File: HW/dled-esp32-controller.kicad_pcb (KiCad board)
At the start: 2 copper layers, 50 x 48 mm, 40 parts, among them J1 PinsI2C, J2 PinsDbg, J3 BootBtn, J4 swRes, J5 LEDcmd, J6 PinsExt, J7 PinsExt2, J8 LEDpwr, J9 Power5V, Q1 STD46P4LLF6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

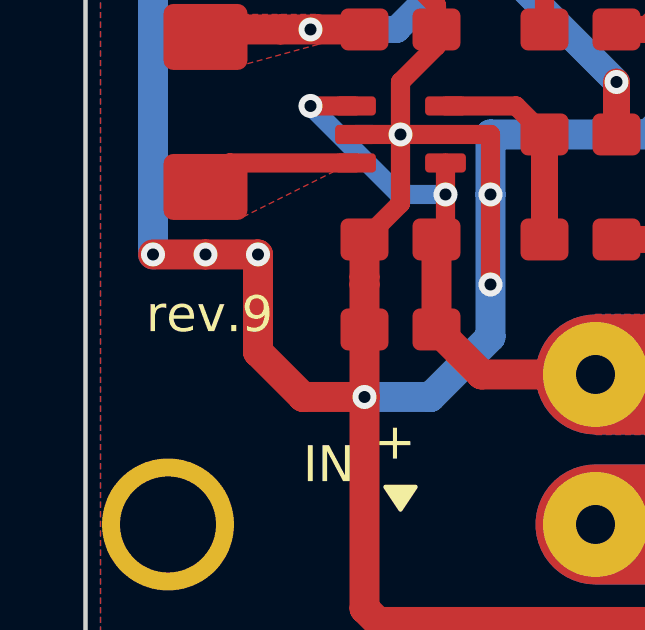
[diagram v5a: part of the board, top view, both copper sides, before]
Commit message: Changes the 3D representation of some connectors
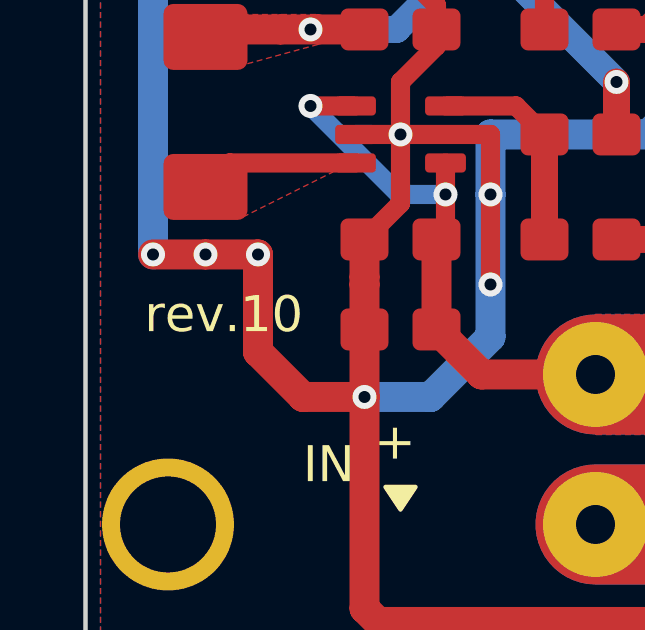
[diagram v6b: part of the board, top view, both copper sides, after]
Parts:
- J2: footprint CalinConnectors:Pin_Header_Straight_1x03 -> CalinConnectors:Pin_Header_Straight_1x03_Cyan
- J5: footprint CalinConnectors:Pin_Header_Straight_1x03 -> CalinConnectors:Pin_Header_Straight_1x03_Yellow
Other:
- board text added: "rev.10"
- board text removed: "rev.9"

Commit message: Rebuilds the PCB for revision 11
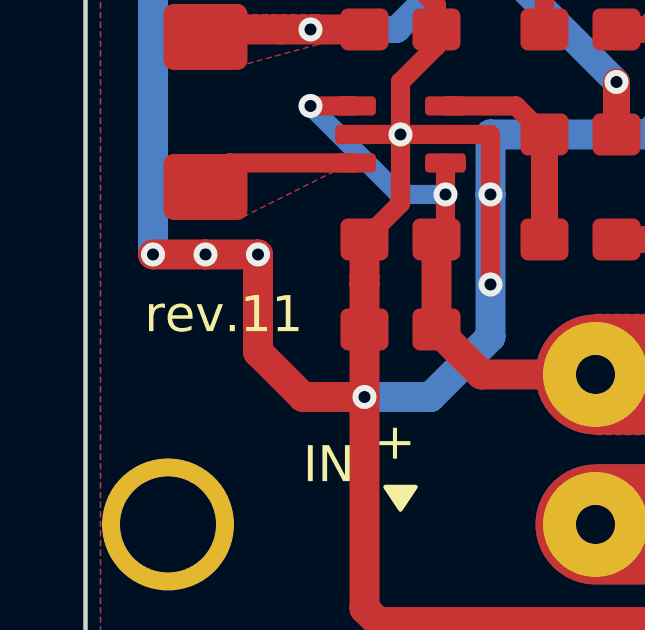
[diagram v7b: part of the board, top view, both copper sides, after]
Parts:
- L1: value 1uH -> 2.2uH
- R2: value 1k -> 330
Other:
- board text added: "rev.11"
- board text removed: "rev.10"
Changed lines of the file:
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@@
       (effects (font (size 1 1) (thickness 0.15)))
     )
-    (fp_text value 1uH (at 0 -3.4 90) (layer F.Fab)
+    (fp_text value 2.2uH (at 0 -3.4 90) (layer F.Fab)
       (effects (font (size 1 1) (thickness 0.15)))
     )
@@
       (effects (font (size 1 1) (thickness 0.15)))
     )
-    (fp_text value 1k (at 0 -2 180) (layer F.Fab)
+    (fp_text value 330 (at 0 -2 180) (layer F.Fab)
       (effects (font (size 1 1) (thickness 0.15)))
     )
@@
     )
   )
-  (gr_text rev.10 (at 32.25 88.5) (layer F.SilkS)
+  (gr_text rev.11 (at 32.25 88.5) (layer F.SilkS)
     (effects (font (size 1.2 1.2) (thickness 0.25)) (justify right))
   )
@@
   (via (at 67 67.7) (size 0.8) (drill 0.4) (layers F.Cu B.Cu) (net 1))
   (segment (start 67 67.7) (end 68.7 67.7) (width 0.9) (layer F.Cu) (net 1))
-  (segment (start 71.24 70.24) (end 73 70.24) (width 0.9) (layer F.Cu) (net 1))
+  (segment (start 71.24 70.24) (end 73 70.24) (width 0.9) (layer F.Cu) (net 1) (status 20))
   (segment (start 68.7 67.7) (end 71.24 70.24) (width 0.9) (layer F.Cu) (net 1))
   (via (at 32.5 59.5) (size 0.8) (drill 0.4) (layers F.Cu B.Cu) (net 2))

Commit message: Updates components to add manufacturer, part number, ... fields, checked the values and adds power flags for a clean ERC test
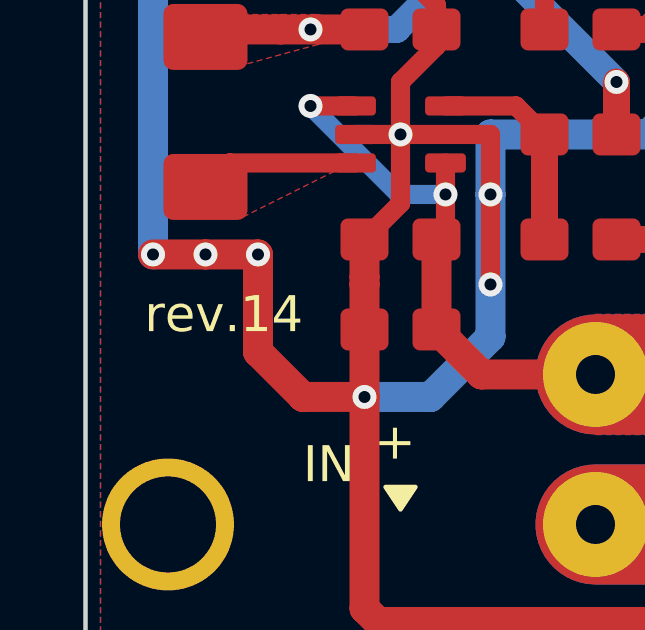
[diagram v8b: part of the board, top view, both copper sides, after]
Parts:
- C7: value 10uF -> 10uF/10V/1mOhm
- C8: value 22uF 1mOhm -> 22uF/6.3V/1mOhm
- J1: value PinsI2C -> CS_4
- J2: value PinsDbg -> CS_3
- J3: value BootBtn -> CS_2
- J4: value swRes -> CS_2
- J5: value LEDcmd -> CS_3
- J6: value PinsExt -> CS_5
- J7: value PinsExt2 -> CS_3
- J8: value LEDpwr -> CS_Pwr
- J9: value Power5V -> CS_Pwr
- R3, R4: value 2K2 -> 2k2
- R8: value 10K -> 10k
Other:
- board text added: "rev.14"
- board text removed: "rev.11"
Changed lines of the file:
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@@
     (user_trace_width 4)
     (trace_clearance 0.3)
-    (zone_clearance 0.7)
+    (zone_clearance 0.8)
     (zone_45_only no)
     (trace_min 0.35)
@@
     (mod_text_size 1 1)
     (mod_text_width 0.15)
-    (pad_size 2.4 2)
-    (pad_drill 1)
+    (pad_size 3.5 3.5)
+    (pad_drill 1.3)
     (pad_to_mask_clearance 0.051)
     (solder_mask_min_width 0.25)
@@
       (effects (font (size 1 1) (thickness 0.15)))
     )
-    (fp_text value LEDcmd (at 2.54 0 90) (layer F.Fab)
+    (fp_text value CS_3 (at 2.54 0 90) (layer F.Fab)
       (effects (font (size 1 1) (thickness 0.15)))
     )
@@
       (effects (font (size 1 1) (thickness 0.15)))
     )
-    (fp_text value PinsDbg (at 2.54 0 90) (layer F.Fab)
+    (fp_text value CS_3 (at 2.54 0 90) (layer F.Fab)
       (effects (font (size 1 1) (thickness 0.15)))
     )
@@
       (effects (font (size 1 1) (thickness 0.15)))
     )
-    (fp_text value LEDpwr (at 0 -1.9 90) (layer F.Fab)
+    (fp_text value CS_Pwr (at 0 -1.9 90) (layer F.Fab)
       (effects (font (size 1 1) (thickness 0.15)))
     )
@@
       (effects (font (size 1 1) (thickness 0.15)))
     )
-    (fp_text value Power5V (at 0 -1.9 270) (layer F.Fab)
+    (fp_text value CS_Pwr (at 0 -1.9 270) (layer F.Fab)
       (effects (font (size 1 1) (thickness 0.15)))
     )
@@
       (effects (font (size 1 1) (thickness 0.15)))
     )
-    (fp_text value PinsExt (at 2.54 3.81 180) (layer F.Fab)
+    (fp_text value CS_5 (at 2.54 3.81 180) (layer F.Fab)
       (effects (font (size 1 1) (thickness 0.15)))
     )
@@
       (effects (font (size 1 1) (thickness 0.15)))
     )
-    (fp_text value 10uF (at 0 -2 180) (layer F.Fab)
+    (fp_text value 10uF/10V/1mOhm (at 0 -2 180) (layer F.Fab)
       (effects (font (size 1 1) (thickness 0.15)))
     )
@@
       (effects (font (size 1 1) (thickness 0.15)))
     )
-    (fp_text value "22uF 1mOhm" (at 0 -2) (layer F.Fab)
+    (fp_text value 22uF/6.3V/1mOhm (at 0 -2) (layer F.Fab)
       (effects (font (size 1 1) (thickness 0.15)))
     )
@@
       (effects (font (size 1 1) (thickness 0.15)))
     )
-    (fp_text value 2K2 (at 0 -2 90) (layer F.Fab)
+    (fp_text value 2k2 (at 0 -2 90) (layer F.Fab)
       (effects (font (size 1 1) (thickness 0.15)))
     )
@@
       (effects (font (size 1 1) (thickness 0.15)))
     )
-    (fp_text value 10K (at 0 -2) (layer F.Fab)
+    (fp_text value 10k (at 0 -2) (layer F.Fab)
       (effects (font (size 1 1) (thickness 0.15)))
     )
@@
       (effects (font (size 1 1) (thickness 0.15)))
     )
-    (fp_text value PinsI2C (at 2.54 3.81 90) (layer F.Fab)
+    (fp_text value CS_4 (at 2.54 3.81 90) (layer F.Fab)
       (effects (font (size 1 1) (thickness 0.15)))
     )
@@
       (effects (font (size 1 1) (thickness 0.15)))
     )
-    (fp_text value 2K2 (at 0 -2 90) (layer F.Fab)
+    (fp_text value 2k2 (at 0 -2 90) (layer F.Fab)
       (effects (font (size 1 1) (thickness 0.15)))
     )
@@
       (effects (font (size 1 1) (thickness 0.15)))
     )
-    (fp_text value BootBtn (at 2.54 0 90) (layer F.Fab)
+    (fp_text value CS_2 (at 2.54 0 90) (layer F.Fab)
       (effects (font (size 1 1) (thickness 0.15)))
     )
@@
       (effects (font (size 1 1) (thickness 0.15)))
     )
-    (fp_text value swRes (at 2.54 0) (layer F.Fab)
+    (fp_text value CS_2 (at 2.54 0) (layer F.Fab)
       (effects (font (size 1 1) (thickness 0.15)))
     )
@@
       (effects (font (size 1 1) (thickness 0.15)))
     )
-    (fp_text value PinsExt2 (at 2.54 0 90) (layer F.Fab)
+    (fp_text value CS_3 (at 2.54 0 90) (layer F.Fab)
       (effects (font (size 1 1) (thickness 0.15)))
     )
@@
     )
   )
-  (gr_text rev.11 (at 32.25 88.5) (layer F.SilkS)
+  (gr_text rev.14 (at 32.25 88.5) (layer F.SilkS)
     (effects (font (size 1.2 1.2) (thickness 0.25)) (justify right))
   )
@@
   (segment (start 56.5 68.5) (end 59.84 65.16) (width 0.9) (layer B.Cu) (net 27))
   (zone (net 1) (net_name GND) (layer B.Cu) (hatch edge 0.508)
-    (connect_pads yes (clearance 0.8))
+    (connect_pads no (clearance 0.8))
     (min_thickness 0.8)
     (fill yes (arc_segments 16) (thermal_gap 0.8) (thermal_bridge_width 0.8))
